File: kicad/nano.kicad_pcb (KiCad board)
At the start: 4 copper layers, 85 x 56 mm, 229 parts, among them J1 SD-104031, J2 PMIC_I2C, J3 USB_Micro, J4 USB_OTG, J5 JTAG, J6 TOUCH PANEL, J7 LiPo_THM, P1 EXPANSION, P2 DISPLAY, P3 J0011D01BNL, P4 USB-A-D-RA-30, P5 USB-A-D-RA-30, Q1 2SK3018, U1 IMX6UL_BGA289, U10 MIC2506, U11 MIC2506, U12 MIC2877, U2 DDR3_BGA96, U3 A7101CH, U4 W25M512JV, U5 W25M512JV, U6 PF1550, U7 LAN8720A, U8 USB2514B, U9 CP2102N-QFN20, Y1 32.768 kHz

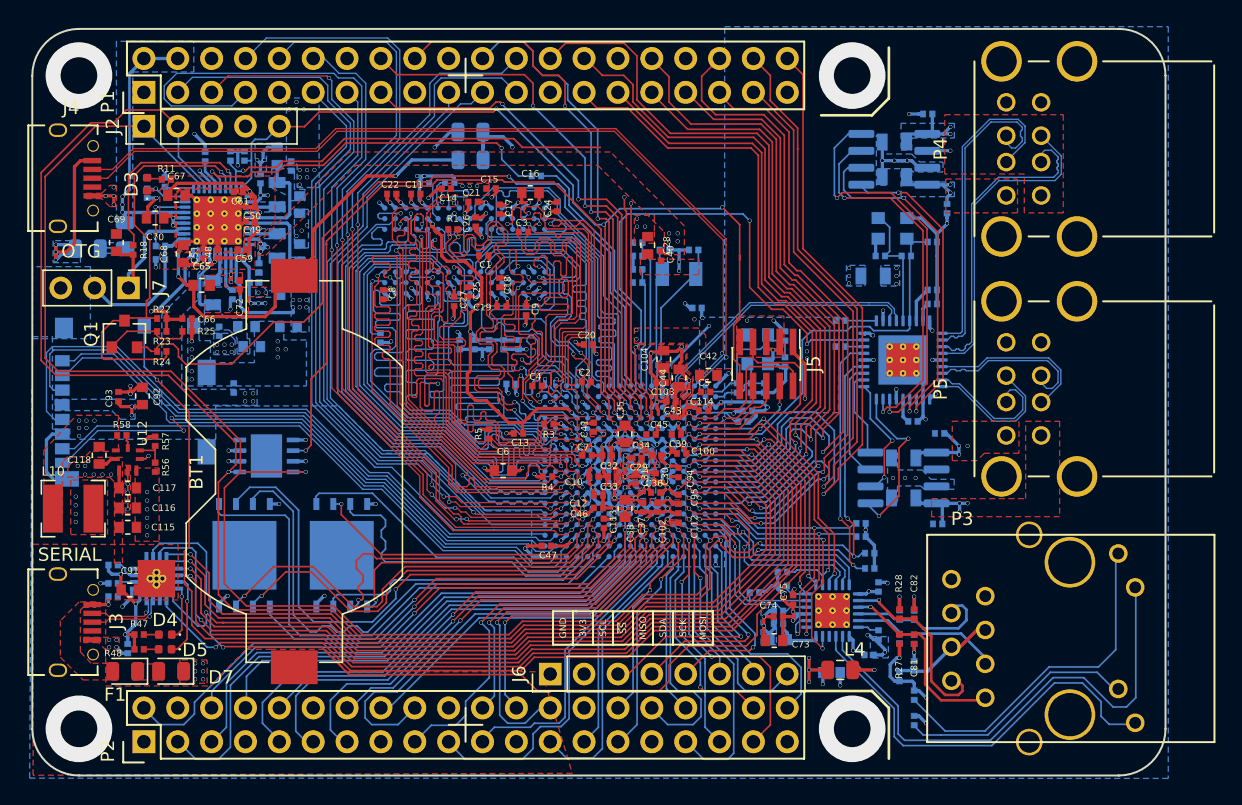
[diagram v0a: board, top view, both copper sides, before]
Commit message: add block diagram
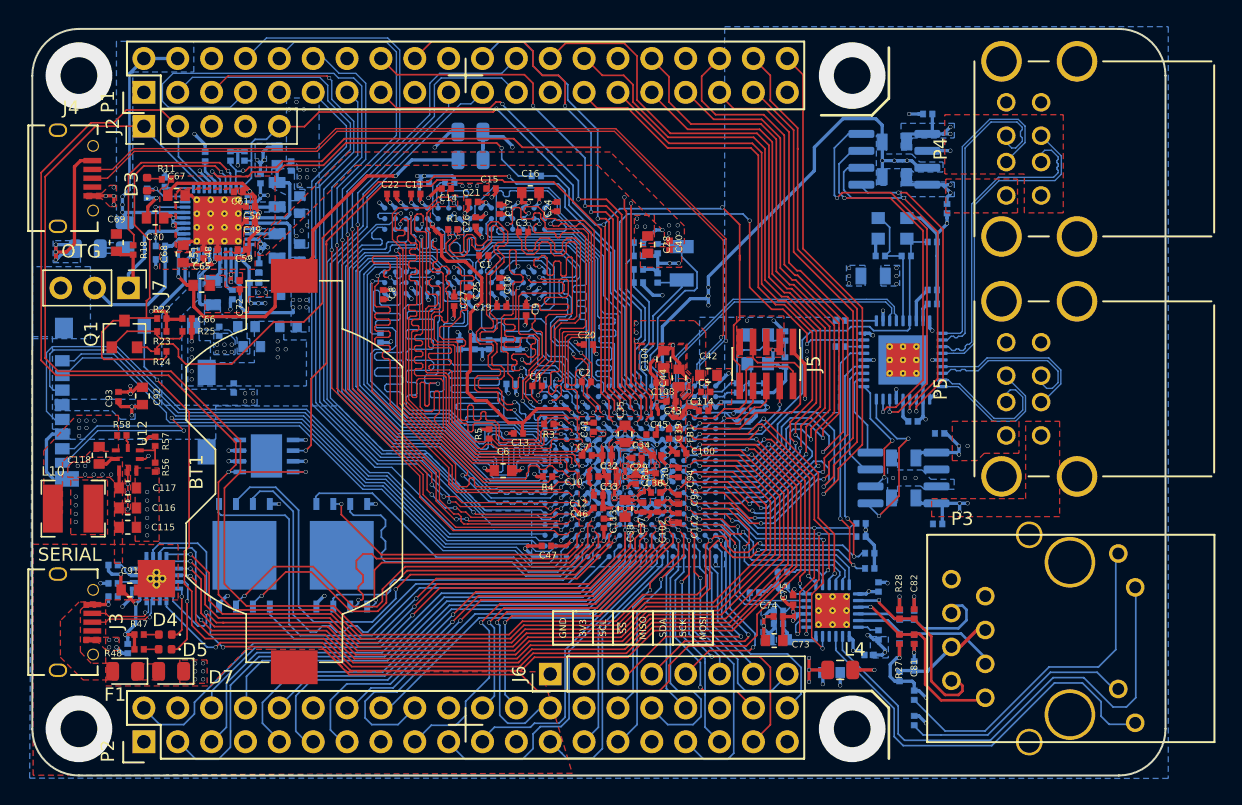
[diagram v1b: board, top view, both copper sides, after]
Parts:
- FB1: moved to F.Cu
- moved FB1 9.54 mm to (158.6, 102.9), turned to 270 degrees
- moved C97 2.70 mm to (156.9, 89.0), turned to 270 degrees
- moved C96 2.16 mm to (156.9, 91.2), turned to 90 degrees
- moved SB2 2.00 mm to (155.5, 89.5), turned to 0 degrees
- moved SB1 2.00 mm to (155.5, 88.5), turned to 0 degrees
- moved SB3 2.00 mm to (155.5, 91.5), turned to 0 degrees
- moved SB4 2.00 mm to (155.5, 90.5), turned to 0 degrees
- moved C40 1.03 mm to (157.8, 88.7)
- moved Y1 0.82 mm to (158.7, 90.1), turned to 270 degrees
- moved C39 0.55 mm to (157.8, 102.9), turned to 270 degrees
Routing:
- net 5V: track 35.5 -> 61.0 mm, vias 23 -> 25
- net /Clock_and_Control/VDDA_ADC: track 18.0 -> 9.06 mm, vias 3 -> 2
- net /Clock_and_Control/RTC_XTALI: track 12.2 -> 15.5 mm
- net VDD_SNVS_IN: track 45.0 -> 41.8 mm, vias 3 -> 4
- net /Clock_and_Control/BOOT1: track 9.01 -> 12.1 mm
- net GND: track 219.0 -> 220.6 mm
- net /Clock_and_Control/BOOT0: track 12.3 -> 10.7 mm
- net HUB_D+: track 20.7 -> 21.8 mm
- net HUB_D-: track 20.9 -> 22.0 mm
- net VDD_HIGH_IN: track 6.60 -> 5.93 mm, vias 10 -> 9
- net CSI_DATA04: track 71.3 -> 71.8 mm
- net /Clock_and_Control/RTC_XTALO: track 10.7 -> 11.2 mm
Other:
- rule pad_to_mask_clearance: 0.08 -> 0.04
- board text added: "CAP 5V USB / GND"

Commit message: layout improvement
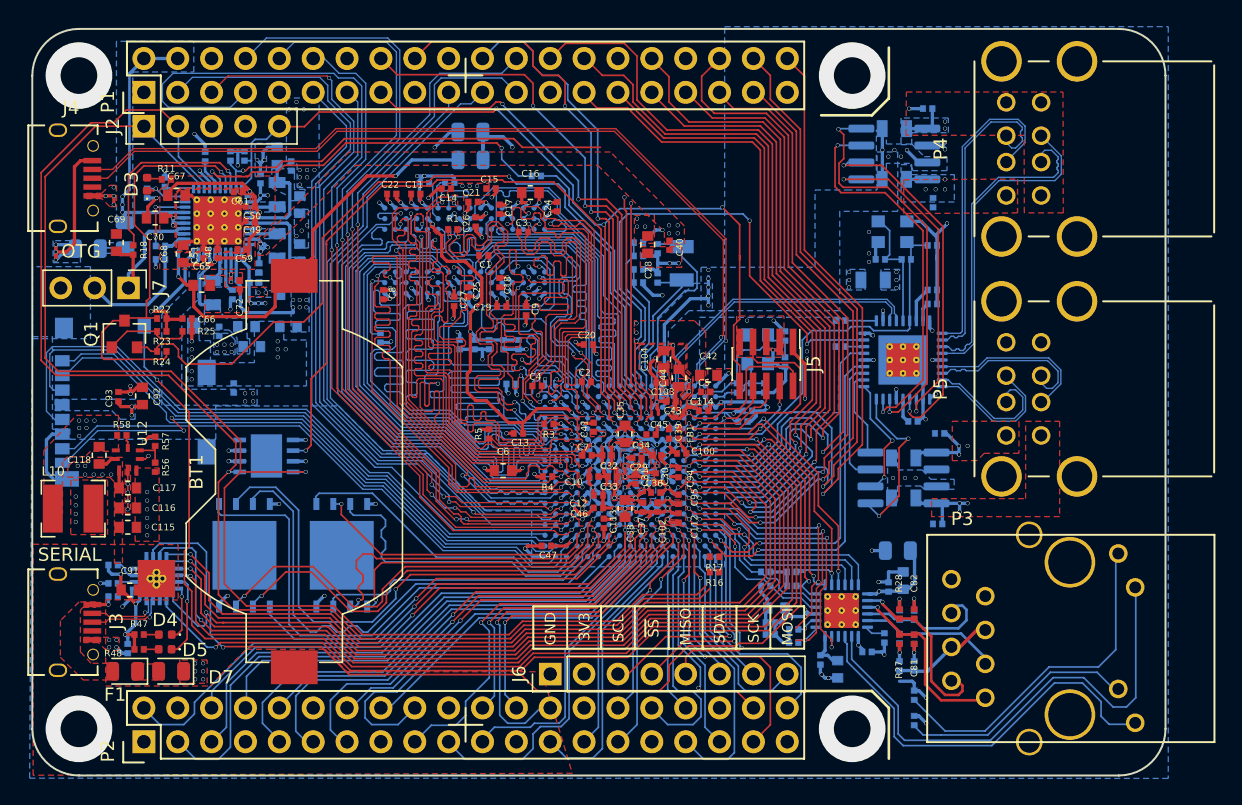
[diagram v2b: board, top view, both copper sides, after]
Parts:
- C73, C74, C75, L4: moved to B.Cu
- R16, R17: moved to F.Cu
- moved R16 11.7 mm to (161.2, 113.2)
- moved R17 11.7 mm to (161.2, 112.1)
- moved L4 9.94 mm to (174.9, 111.6)
- moved R36 9.42 mm to (167.1, 117.5), turned to 180 degrees
- moved R37 9.42 mm to (167.1, 118.5), turned to 180 degrees
- moved C78 8.75 mm to (175.3, 113.9), turned to 90 degrees
- moved C77 4.96 mm to (170.4, 120.5), turned to 270 degrees
- moved C76 4.15 mm to (169.1, 119.8), turned to 270 degrees
- moved C75 3.11 mm to (165.4, 117.9), turned to 180 degrees
- moved C73 2.45 mm to (165.8, 115.9)
- moved R39 2.11 mm to (165.0, 114.3)
- moved R38 1.77 mm to (165.0, 113.2)
- moved C105 1.14 mm to (177.6, 85.5)
- moved L6 1.00 mm to (174.7, 80.0)
- moved R31 0.80 mm to (175.0, 120.3), turned to 270 degrees
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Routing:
- net 5V: track 61.0 -> 38.4 mm, vias 25 -> 29
- net BOARD_SCL: track 137.5 -> 128.4 mm, vias 5 -> 3
- net BOARD_SDA: track 134.9 -> 127.7 mm, vias 5 -> 3
- net DCDC_3V3: track 45.7 -> 39.4 mm, vias 33 -> 29
- net /USB HUB/USB0_VBUS: track 5.37 -> 2.10 mm, vias 2 -> 4
- net ETH_RXD0: track 22.4 -> 19.5 mm, vias 2 -> 3
- net GND: track 220.6 -> 217.8 mm, vias 145 -> 146
- net /USB HUB/USB1_VBUS: track 5.89 -> 3.64 mm
- net /USB HUB/PORT1_PWR: track 23.2 -> 25.2 mm
- net DBG_GPIO0: track 68.3 -> 69.9 mm
- net SD1_CD_B: track 86.6 -> 88.0 mm
- net /USB HUB/PORT1_OCS: track 26.2 -> 27.6 mm
- net /IMX_Peripherals_1/TOUCH_SS0: track 18.5 -> 17.2 mm
- net /IMX_Peripherals_1/TOUCH_SCL: track 18.0 -> 16.8 mm
- net /USB HUB/PORT2_OCS: track 27.6 -> 28.8 mm
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
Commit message: add i2c for ULZ
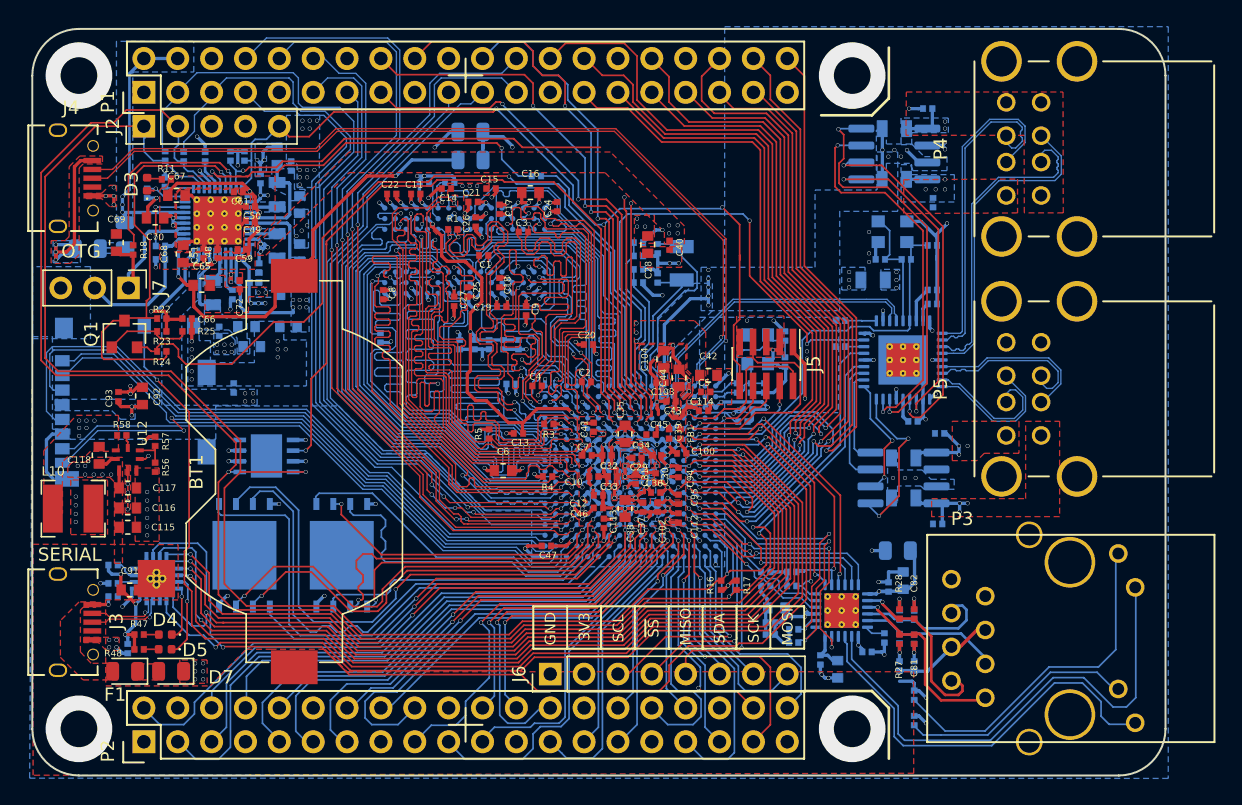
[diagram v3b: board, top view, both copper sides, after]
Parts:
- added SB5: 0, Custom Components:R_0402_narrow, B.Cu at (120.0, 82.0)
- added SB6: 0, Custom Components:R_0402_narrow, B.Cu at (121.4, 82.1)
- moved R17 2.70 mm to (162.8, 114.2), turned to 270 degrees
- moved R16 1.11 mm to (161.7, 114.2), turned to 90 degrees
- moved C101 0.12 mm to (163.7, 101.0)
- moved FB1 0.05 mm to (158.6, 102.9)
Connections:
- P1 pad 11: CSI_DATA06 -> CSI_DATA04
- P1 pad 7: CSI_DATA04 -> CSI_DATA06
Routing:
- net CSI_DATA04: track 71.8 -> 53.0 mm
- net BOARD_SCL: track 128.4 -> 135.6 mm
- net UART2_RXD: track 54.2 -> 47.4 mm
- net CSI_VSYNC: track 59.3 -> 64.8 mm
- net CSI_HSYNC: track 57.8 -> 62.6 mm, vias 3 -> 2
- net BOARD_SDA: track 127.7 -> 132.0 mm
- net CSI_DATA06: track 48.7 -> 52.6 mm
- net UART2_TXD: track 50.2 -> 46.4 mm
- net UART2_CTS: track 51.6 -> 48.3 mm
- net /IMX_Peripherals_1/UART3_RTS: track 46.0 -> 44.5 mm
- net DCDC_3V3: track 39.4 -> 40.8 mm, vias 29 -> 31
- net /IMX_Peripherals_1/UART3_TX: track 46.1 -> 44.8 mm
- net UART2_RTS: track 47.7 -> 46.4 mm
- net ETH_TXEN: track 16.3 -> 15.2 mm
- net DBG_GPIO1: track 66.1 -> 67.1 mm
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- added copper zone on F.Cu, net OTG_VBUS

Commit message: pmic_int connection
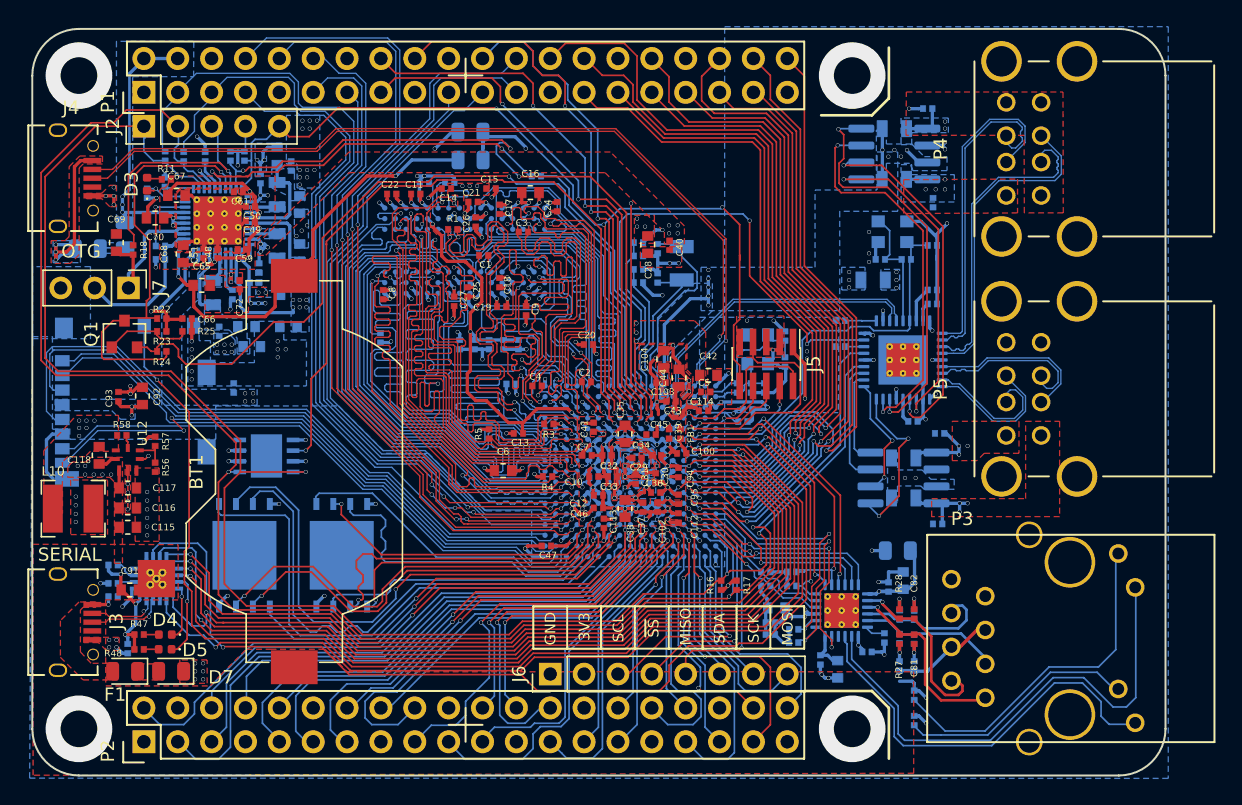
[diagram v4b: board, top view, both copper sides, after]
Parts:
- U9: footprint Package_DFN_QFN:SiliconLabs_QFN-20-1EP_3x3mm_P0.5mm_ThermalVias -> Custom Components:SiliconLabs_QFN-20-1EP_3x3mm_CUSTOM
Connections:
- J2 pad 3: Net-(J2-Pad3) -> /PMIC PF1550/ON_KEY
- J2 pad 4: Net-(J2-Pad4) -> VDD_SNVS
- R19 pad 1: /PMIC PF1550/AUD_INT -> PMIC_INT
- U1 pad N10: /Clock_and_Control/SNVS7 -> PMIC_INT
- U6 pad 9: /PMIC PF1550/AUD_INT -> PMIC_INT
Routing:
- net PMIC_INT: track 0.00 -> 54.5 mm, vias 0 -> 4
- net /PMIC PF1550/AUD_INT: track 30.8 -> 0.00 mm, vias 1 -> 0
- net /Clock_and_Control/SNVS7: track 18.2 -> 0.00 mm, vias 2 -> 0
- net /PMIC PF1550/ON_KEY: track 14.9 -> 18.8 mm
- net VDD_SNVS: track 48.4 -> 50.3 mm
- net SNVS0: track 38.1 -> 39.3 mm
- net /PMIC PF1550/POWERON: track 28.2 -> 27.6 mm

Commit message: remove vsnvs diodes
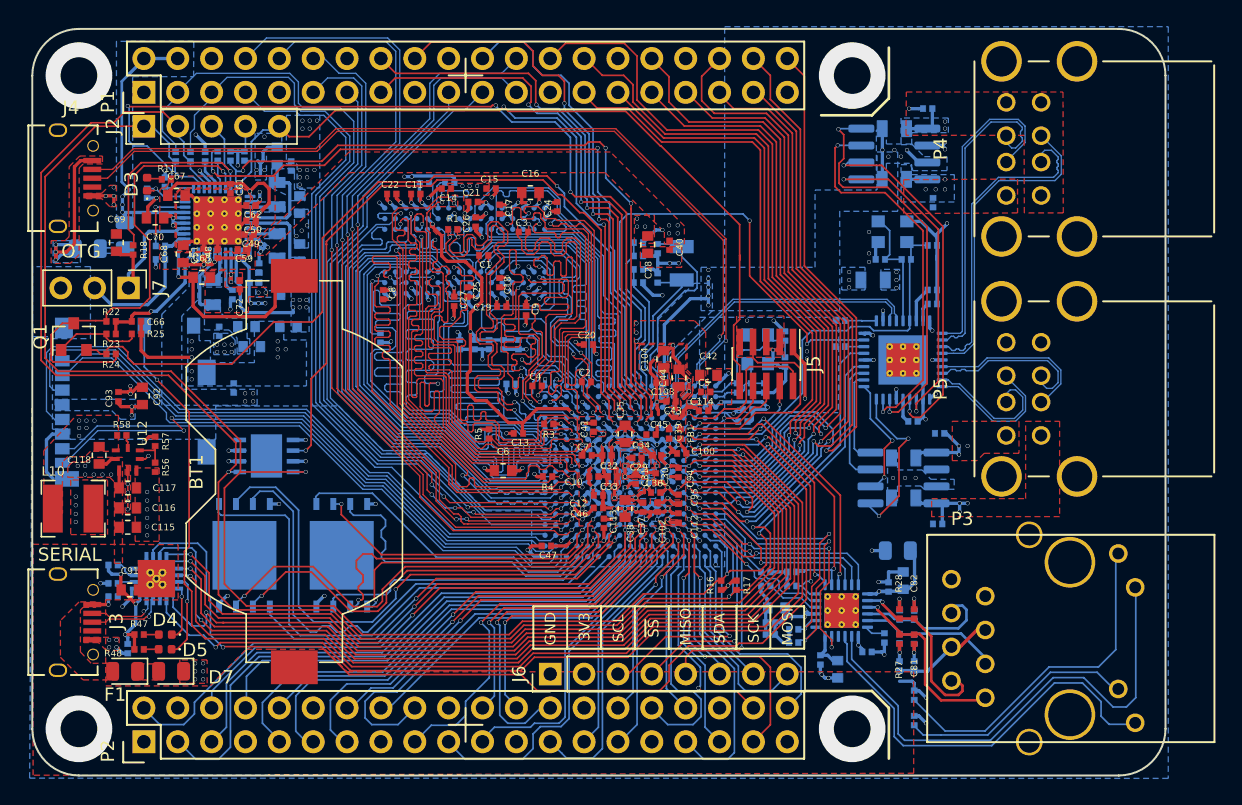
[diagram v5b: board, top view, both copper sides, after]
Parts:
- removed D1, D2: D_Schottky_ALT, Diode_SMD:D_0805_2012Metric
- C62: moved to F.Cu
- moved R41 23.9 mm to (123.9, 82.0), turned to 90 degrees
- moved C66 3.81 mm to (117.8, 94.4)
- moved Q1 3.81 mm to (113.1, 95.6)
- moved R22 3.81 mm to (115.9, 94.4)
- moved R23 3.81 mm to (115.9, 95.4)
- moved R24 3.81 mm to (115.9, 96.9)
- moved R25 3.81 mm to (117.8, 95.4)
- moved C62 2.12 mm to (126.4, 85.7), turned to 180 degrees
- moved C49 1.05 mm to (126.3, 87.9)
- moved C50 1.05 mm to (126.4, 86.9)
- moved SB5 0.80 mm to (120.8, 82.1)
- moved C61 0.65 mm to (124.9, 84.5), turned to 270 degrees
- moved C65 0.60 mm to (122.7, 91.1)
- moved SB6 0.50 mm to (121.9, 82.1)
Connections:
- C114 pad 1: VDD_SNVS_IN -> VDD_SNVS
- SB1 pad 2: VDD_SNVS_IN -> VDD_SNVS
- SB3 pad 2: VDD_SNVS_IN -> VDD_SNVS
- U1 pad N10: PMIC_INT -> PMIC_WDI
- U1 pad P11: /Clock_and_Control/SNVS2 -> PMIC_INT
- U1 pad P12: VDD_SNVS_IN -> VDD_SNVS
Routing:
- net PMIC_WDI: track 2.16 -> 70.5 mm, vias 0 -> 4
- net VDD_SNVS_IN: track 41.0 -> 0.00 mm, vias 4 -> 0
- net VDD_SNVS: track 50.3 -> 88.9 mm, vias 3 -> 5
- net PMIC_ON_REQ: track 20.3 -> 51.8 mm, vias 0 -> 2
- net /PMIC PF1550/POWERON: track 27.6 -> 2.13 mm, vias 2 -> 0
- net /Clock_and_Control/SNVS2: track 16.7 -> 0.00 mm, vias 2 -> 0
- net LICELL: track 32.8 -> 16.0 mm, vias 2 -> 1
- net POR_B: track 75.8 -> 88.2 mm, vias 4 -> 3
- net GND: track 218.0 -> 222.5 mm, vias 146 -> 147
- net PMIC_STBY_REQ: track 59.4 -> 63.0 mm
- net SNVS0: track 39.3 -> 41.8 mm
- net /PMIC PF1550/STANDBY: track 31.7 -> 33.9 mm
- net VSYS: track 26.8 -> 29.1 mm
- net PMIC_INT: track 54.5 -> 52.8 mm
- net BOARD_SDA: track 132.0 -> 131.0 mm
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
